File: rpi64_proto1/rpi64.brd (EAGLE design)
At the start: 100 x 80 mm, 67 parts, among them Q1 BSS123, Q2 BSS123

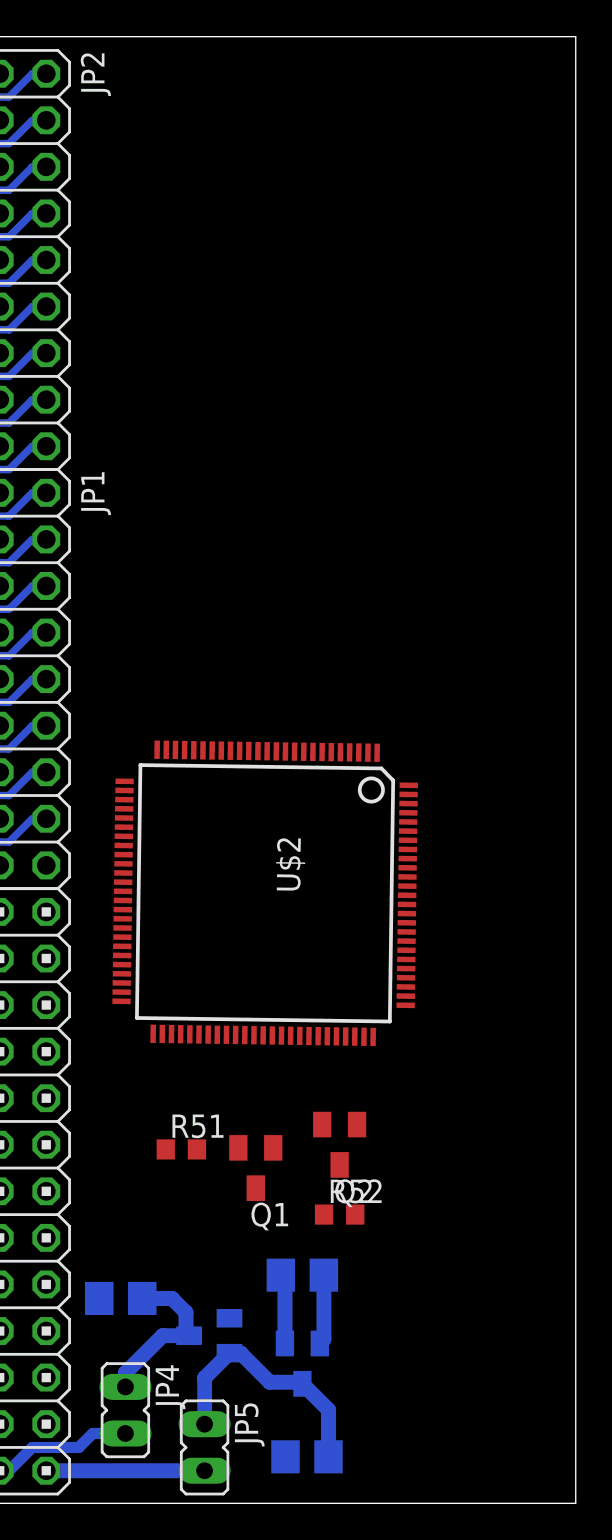
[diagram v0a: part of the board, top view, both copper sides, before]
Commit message: Added front connectors
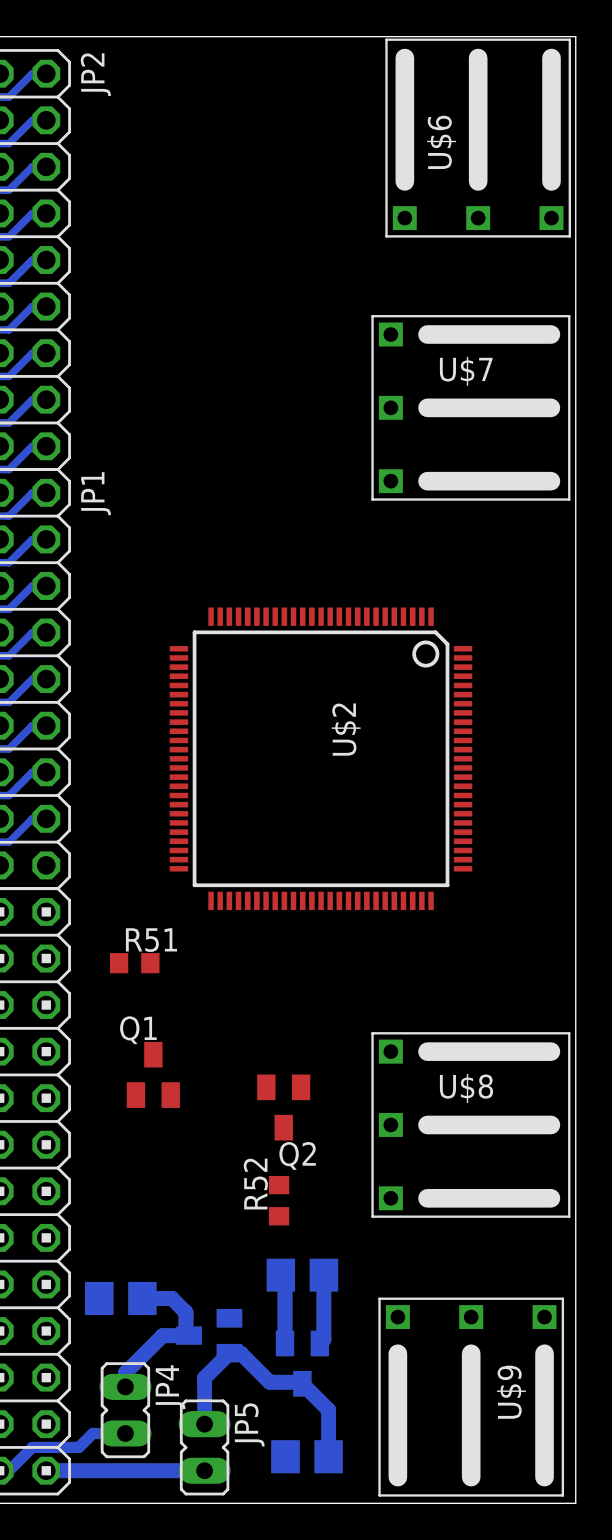
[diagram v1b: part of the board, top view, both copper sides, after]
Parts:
- added U$6, U$7, U$8, U$9: N64_CONTROLER, rpi64:N64_CONTROLER
- moved R51 10.5 mm to (75.9, 29.5)
- moved U$2 7.95 mm to (86.1, 40.6), turned to 270 degrees
- moved Q1 7.55 mm to (77.0, 23.4), turned to 0 degrees
- moved Q2 3.66 mm to (84.1, 21.6)
- moved R52 3.39 mm to (83.8, 16.5), turned to 90 degrees
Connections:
- new net SIG: U$6.P$2, U$7.P$2, U$8.P$2, U$9.P$2
- new net VCC: U$6.P$3, U$7.P$3, U$8.P$3, U$9.P$3
- net GND: now also U$6.P$1, U$7.P$1, U$8.P$1, U$9.P$1

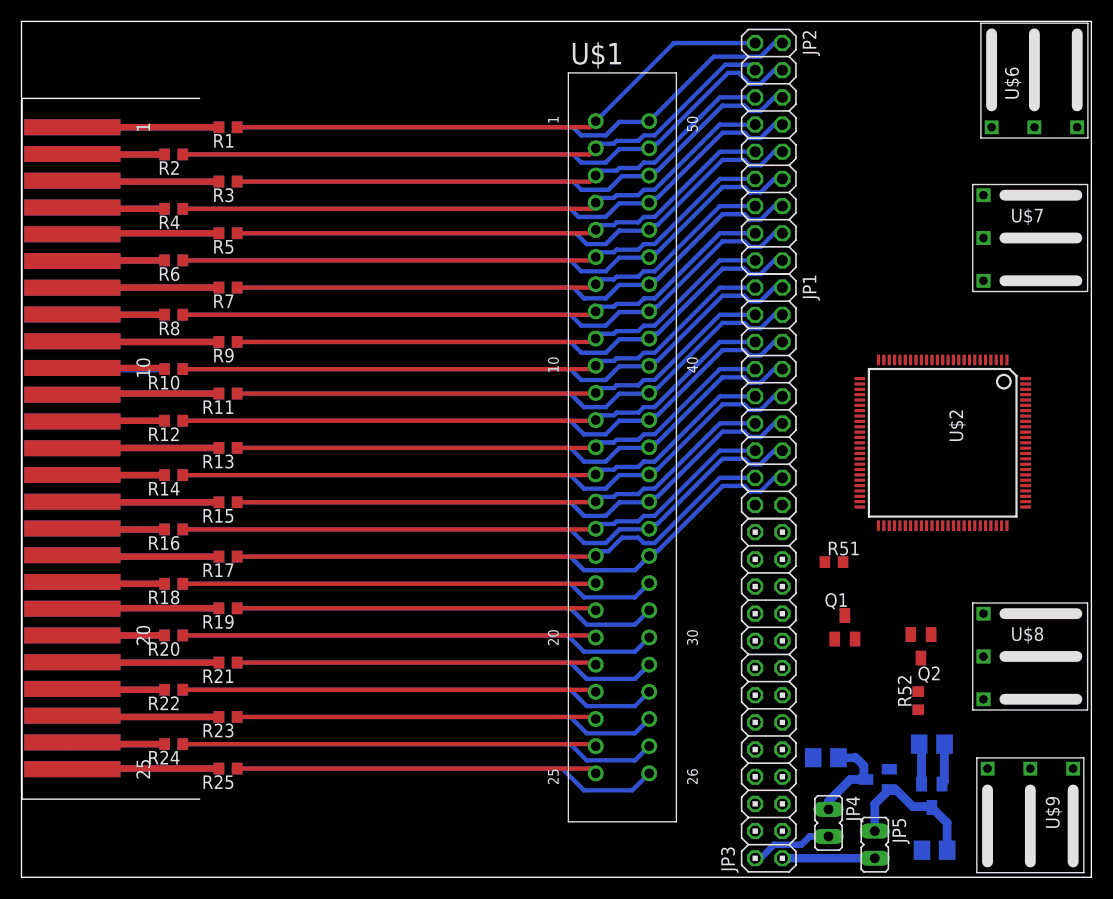
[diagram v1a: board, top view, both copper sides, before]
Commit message: Top layer of resistor placed
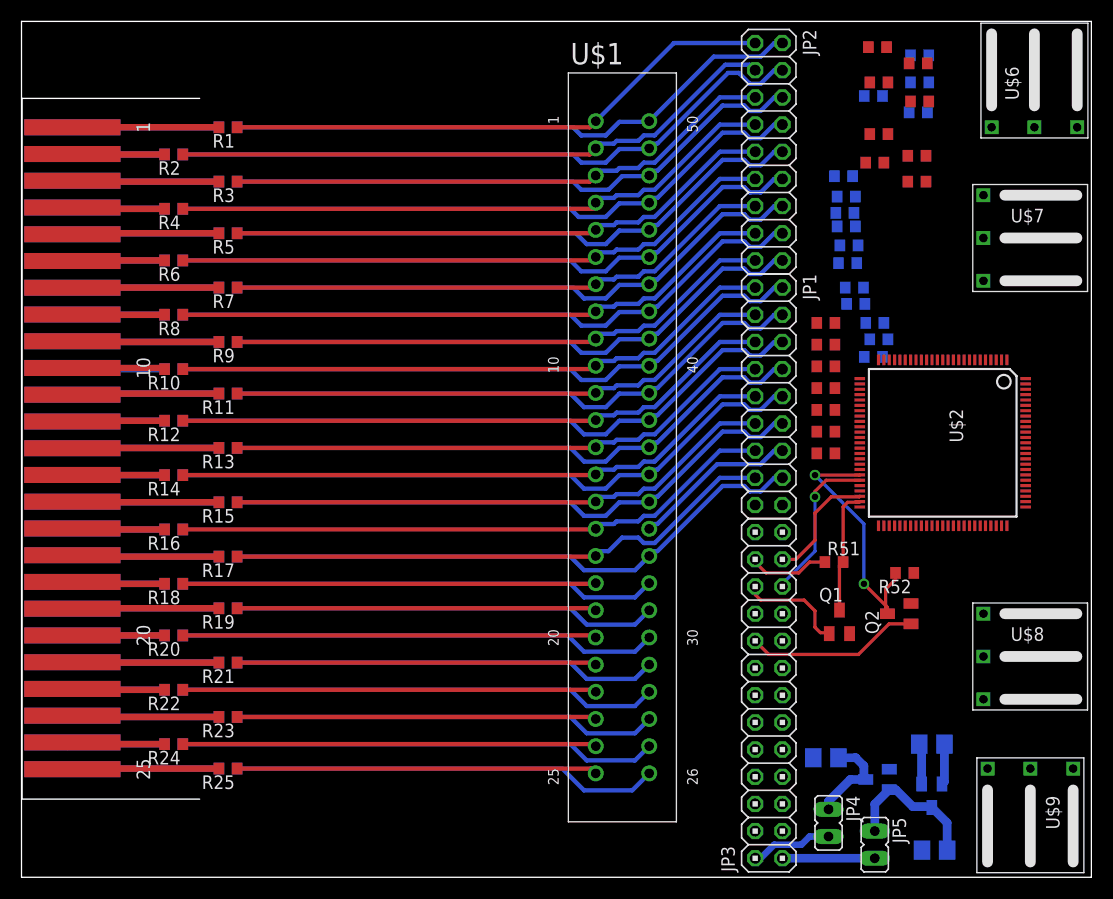
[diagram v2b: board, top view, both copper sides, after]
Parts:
- added R53, R54, R55, R56, R57, R58, R59, R60, R61, R62, R63, R64, R65, R66, R67, R72, R73, R74, R75, R76, R77, R78, R79, R80, R81, R82, R83, R84, R85, R86: (no value), rcl:R0603
- moved R52 12.0 mm to (82.5, 28.4), turned to 180 degrees
- moved Q2 3.66 mm to (82.0, 24.6), turned to 90 degrees
- moved Q1 0.72 mm to (76.5, 23.9)
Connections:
- new net N$104: U$2.24
- new net N$105: JP1.14, R35.2, R85.1, U$1.P$35
- new net N$107: U$2.4
- new net N$109: U$2.18
- new net N$110: U$2.96
- new net N$111: U$2.10
- new net N$112: U$2.16
- new net N$113: U$2.15
- new net N$114: U$2.13
- new net N$115: U$2.12
- new net N$116: U$2.9
- new net N$117: U$2.19
- new net N$118: U$2.20
- new net N$119: U$2.21
- new net N$120: U$2.8
- new net N$121: U$2.7
- new net N$122: U$2.3
- new net N$123: U$2.2
- new net SLOT_0: R67.2, U$2.90
- new net SLOT_1: R66.2, U$2.91
- new net SLOT_10: R57.2, U$2.28
- new net SLOT_11: R56.2, U$2.29
- new net SLOT_12: R55.2, U$2.30
- new net SLOT_13: R54.2, U$2.36
- new net SLOT_14: R53.2, U$2.37
- new net SLOT_2: R65.2, U$2.94
- new net SLOT_3: R64.2, U$2.95
- new net SLOT_4: R63.2, U$2.97
- new net SLOT_5: R62.2, U$2.99
- new net SLOT_6: R61.2, U$2.100
- new net SLOT_7: R60.2, U$2.1
- new net SLOT_8: R59.2, U$2.26
- new net SLOT_9: R58.2, U$2.27
- net N$53: now also R67.1
- net N$54: now also R66.1
- net N$55: now also R65.1
- net N$56: now also R64.1
- net N$57: now also R63.1
- net N$58: now also R62.1
- net N$59: now also R61.1
- net N$60: now also R60.1
- net N$61: now also R59.1
- net N$62: now also R58.1
- net N$63: now also R57.1
- net N$64: now also R56.1
- net N$65: now also R55.1
- net N$66: now also R54.1
- net N$67: now also R53.1
- net N$78: now also R72.1
- net N$79: now also R73.1
- net N$80: now also R74.1
- net N$81: now also R75.1
- net N$82: now also R76.1
- net N$83: now also R77.1
- net N$84: now also R78.1
- net N$85: now also R79.1
- net N$86: now also R80.1
- net N$87: now also R81.1
- net N$88: now also R82.1
- net N$89: now also R83.1
- net N$90: now also R84.1
- net N$91: now also U$2.25; no longer JP1.14, R35.2, U$1.P$35
- net N$92: now also R86.1
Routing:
- net N$91: track 60.7 -> 0.00 mm
- net N$103: track 0.00 -> 24.2 mm, vias 0 -> 2
- net RPI_GPIO24: track 0.00 -> 16.3 mm
- net N$105: track 0.00 -> 15.6 mm
- net RPI_MISO: track 0.00 -> 14.8 mm, vias 0 -> 1
- net N$106: track 0.00 -> 11.6 mm
- net RPI_SCLK: track 0.00 -> 11.2 mm
- net RPI_GPIO25: track 0.00 -> 10.1 mm
- net RPI_CE#: track 0.00 -> 7.61 mm

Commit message: Placed and routed all resistor for N64 slot
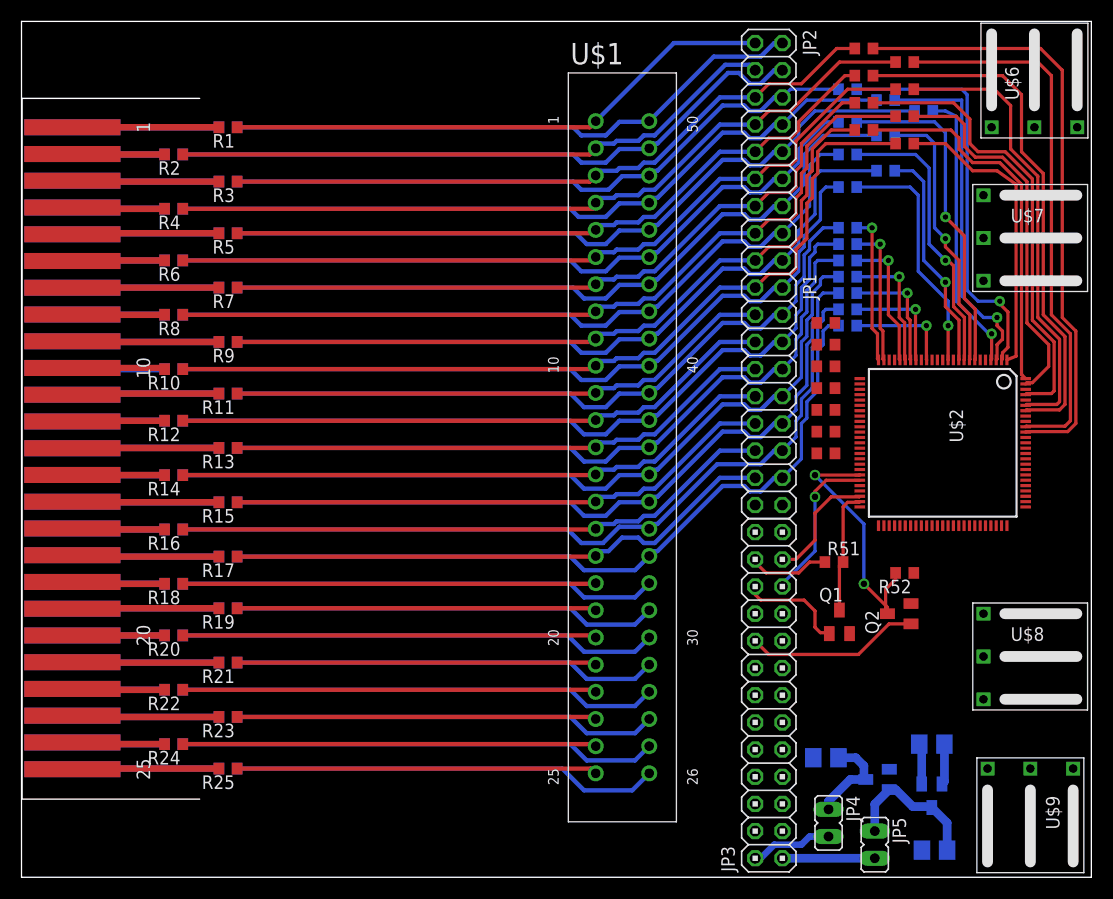
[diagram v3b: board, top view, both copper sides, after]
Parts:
- moved R72 7.44 mm to (77.2, 73.7)
- moved R75 6.66 mm to (77.2, 70.6)
- moved R76 5.48 mm to (80.8, 69.3), turned to 180 degrees
- moved R78 5.48 mm to (80.8, 66.0), turned to 180 degrees
- moved R74 4.90 mm to (84.3, 71.6)
- moved R85 4.04 mm to (77.2, 53.1), turned to 180 degrees
- moved R77 3.94 mm to (77.2, 67.6), turned to 180 degrees
- moved R62 3.86 mm to (82.5, 71.1)
- moved R86 3.79 mm to (77.2, 51.6), turned to 180 degrees
- moved R84 3.78 mm to (77.2, 54.6), turned to 180 degrees
- moved R60 3.74 mm to (82.5, 68.6)
- moved R79 3.69 mm to (77.2, 64.5), turned to 180 degrees
- moved R73 3.58 mm to (80.8, 72.6)
- moved R63 3.24 mm to (78.7, 72.4)
- moved R61 3.21 mm to (78.7, 69.8)
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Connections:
- removed net N$104: U$2.24
- removed net N$107: U$2.4
- removed net N$109: U$2.18
- removed net N$111: U$2.10
- removed net N$112: U$2.16
- removed net N$115: U$2.12
- removed net N$116: U$2.9
- removed net N$117: U$2.19
- removed net N$118: U$2.20
- removed net N$119: U$2.21
- removed net N$120: U$2.8
- removed net N$121: U$2.7
- removed net N$122: U$2.3
- removed net N$123: U$2.2
- removed net N$91: U$2.25
- new net SLOT_15: R86.2, U$2.16
- new net SLOT_16: R85.2, U$2.18
- new net SLOT_17: R84.2, U$2.19
- new net SLOT_18: R83.2, U$2.20
- new net SLOT_19: R82.2, U$2.21
- new net SLOT_20: R81.2, U$2.24
- new net SLOT_21: R80.2, U$2.25
- new net SLOT_22: R79.2, U$2.12
- new net SLOT_23: R78.2, U$2.10
- new net SLOT_24: R77.2, U$2.9
- new net SLOT_25: R76.2, U$2.8
- new net SLOT_26: R75.2, U$2.7
- new net SLOT_27: R74.2, U$2.4
- new net SLOT_28: R73.2, U$2.3
- new net SLOT_29: R72.2, U$2.2
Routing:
- net N$105: track 15.6 -> 76.4 mm
- net SLOT_0: track 0.00 -> 57.1 mm
- net SLOT_1: track 0.00 -> 50.8 mm
- net SLOT_2: track 0.00 -> 49.2 mm
- net SLOT_4: track 0.00 -> 42.6 mm
- net SLOT_3: track 0.00 -> 42.6 mm
- net SLOT_29: track 0.00 -> 38.3 mm, vias 0 -> 1
- net SLOT_5: track 0.00 -> 35.2 mm
- net SLOT_6: track 0.00 -> 34.9 mm
- net SLOT_28: track 0.00 -> 33.1 mm, vias 0 -> 1
- net SLOT_26: track 0.00 -> 31.1 mm, vias 0 -> 1
- net SLOT_7: track 0.00 -> 28.0 mm
- net SLOT_24: track 0.00 -> 26.8 mm, vias 0 -> 1
- net SLOT_27: track 0.00 -> 26.6 mm, vias 0 -> 1
- net SLOT_25: track 0.00 -> 25.6 mm, vias 0 -> 1
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
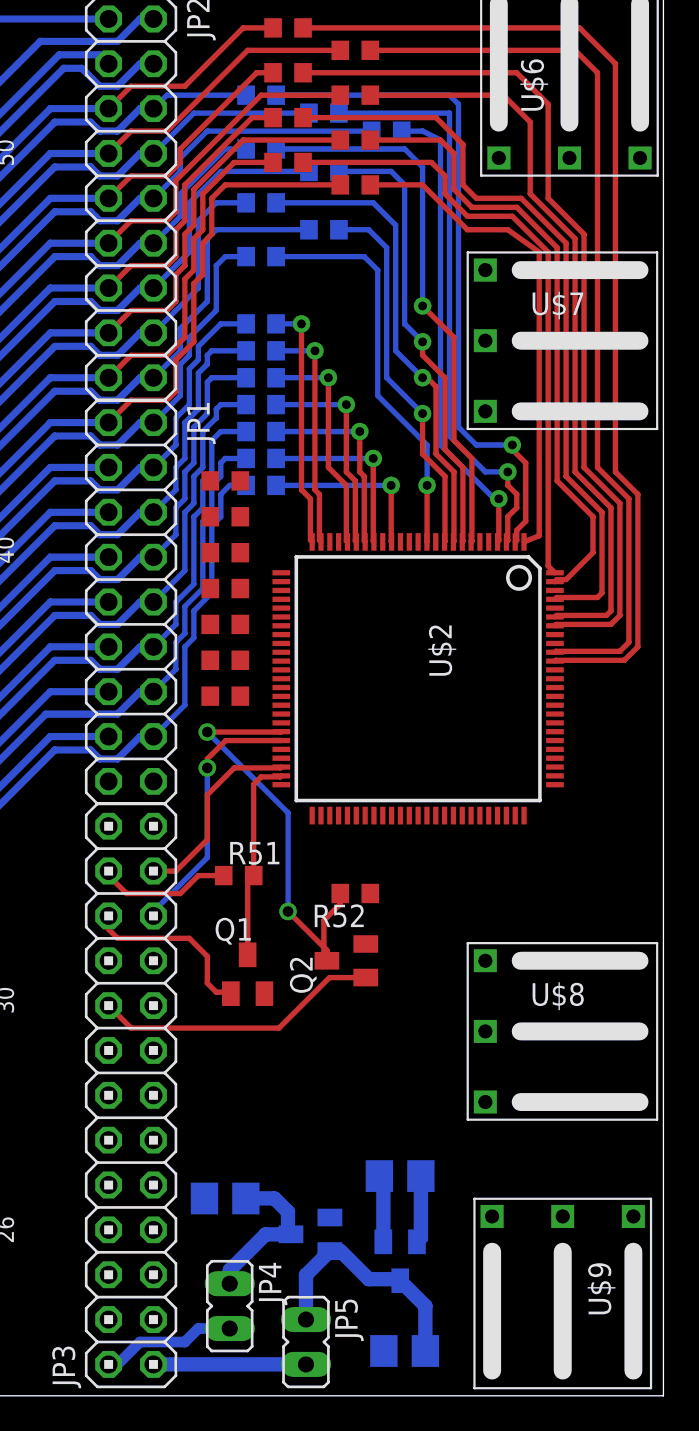
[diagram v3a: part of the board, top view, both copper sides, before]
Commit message: Added decoupling capacitors
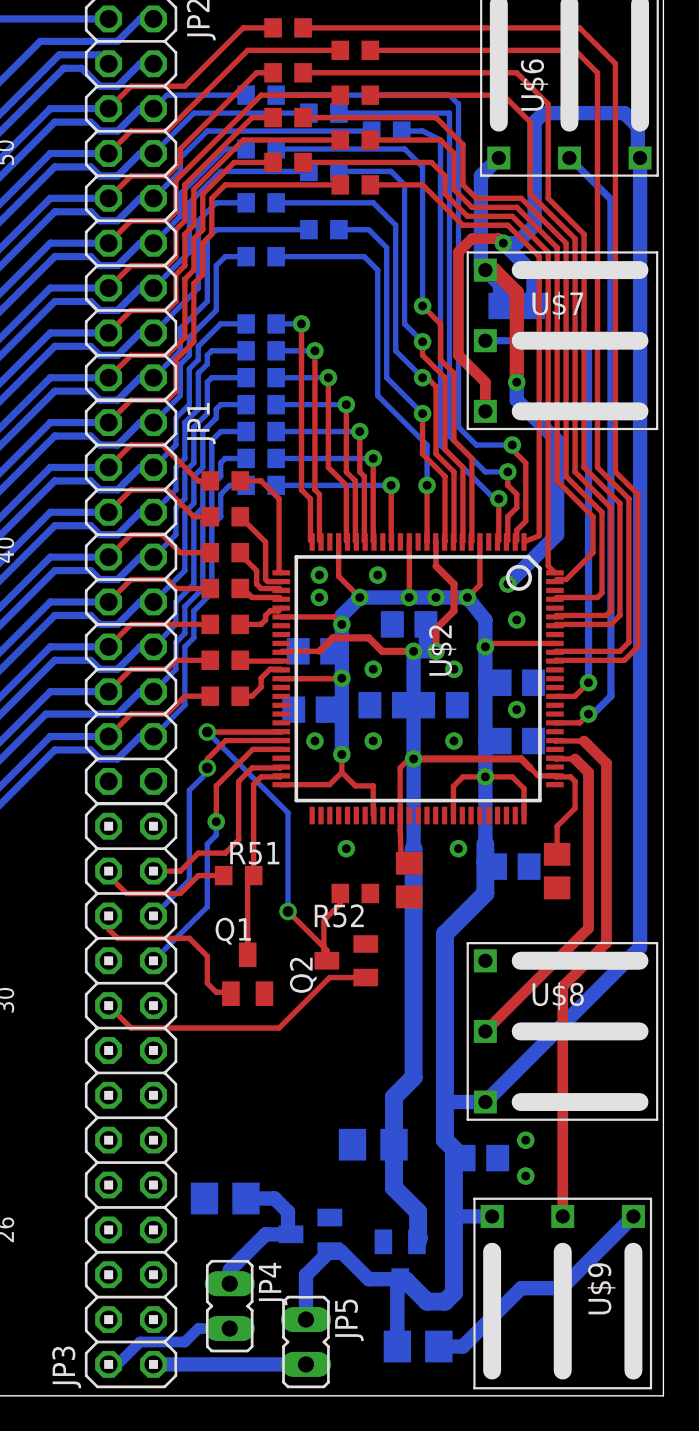
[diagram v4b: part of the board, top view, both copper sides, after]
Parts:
- added C10, C11, C12, C13, C14, C15, C4, C5, C6, C7, C8, C9: (no value), rcl:C0805
- moved C3 2.34 mm to (83.6, 14.2)
- moved C2 0.80 mm to (86.1, 2.79), turned to 0 degrees
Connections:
- removed net SIG: U$6.P$2, U$7.P$2, U$8.P$2, U$9.P$2
- removed net VCC: U$6.P$3, U$7.P$3, U$8.P$3, U$9.P$3
- new net CTRL0: U$2.83, U$6.P$2
- new net CTRL1: U$2.86, U$7.P$2
- new net CTRL2: U$2.79, U$8.P$2
- new net CTRL3: U$2.81, U$9.P$2
- net +3V3: now also C14.1, C4.1, C5.1, C6.1, C7.1, C8.1, C9.1, U$6.P$3, U$7.P$3, U$8.P$3, U$9.P$3; no longer U$2.11, U$2.35, U$2.61, U$2.77
- net GND: now also C10.2, C11.2, C12.2, C13.2, C14.2, C15.2, C4.2, C5.2, C6.2, C7.2, C8.2, C9.2
- net V1V2: now also C10.1, C11.1, C12.1, C13.1, C15.1, U$2.11, U$2.35, U$2.61, U$2.77
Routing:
- net +3V3: track 13.7 -> 209.0 mm, vias 0 -> 10
- net V1V2: track 3.82 -> 75.1 mm, vias 0 -> 3
- net GND: track 3.82 -> 44.2 mm, vias 0 -> 16
- net CTRL0: track 0.00 -> 35.3 mm, vias 0 -> 1
- net CTRL3: track 0.00 -> 30.1 mm
- net CTRL1: track 0.00 -> 27.1 mm, vias 0 -> 1
- net CTRL2: track 0.00 -> 19.3 mm
- net RPI_MOSI: track 0.00 -> 15.9 mm, vias 0 -> 1
- net N$61: track 51.5 -> 58.6 mm
- net N$62: track 56.6 -> 63.5 mm
- net SLOT_8: track 0.00 -> 6.86 mm
- net N$67: track 51.9 -> 58.6 mm
- net N$63: track 51.5 -> 58.2 mm
- net N$66: track 56.6 -> 63.1 mm
- net N$64: track 56.6 -> 63.1 mm
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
